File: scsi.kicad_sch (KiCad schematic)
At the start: 66 parts, among them IC107 D4364G, IC109 D6378GF, IC301 L7805, IC302 1951A, Q104 2SC2412K

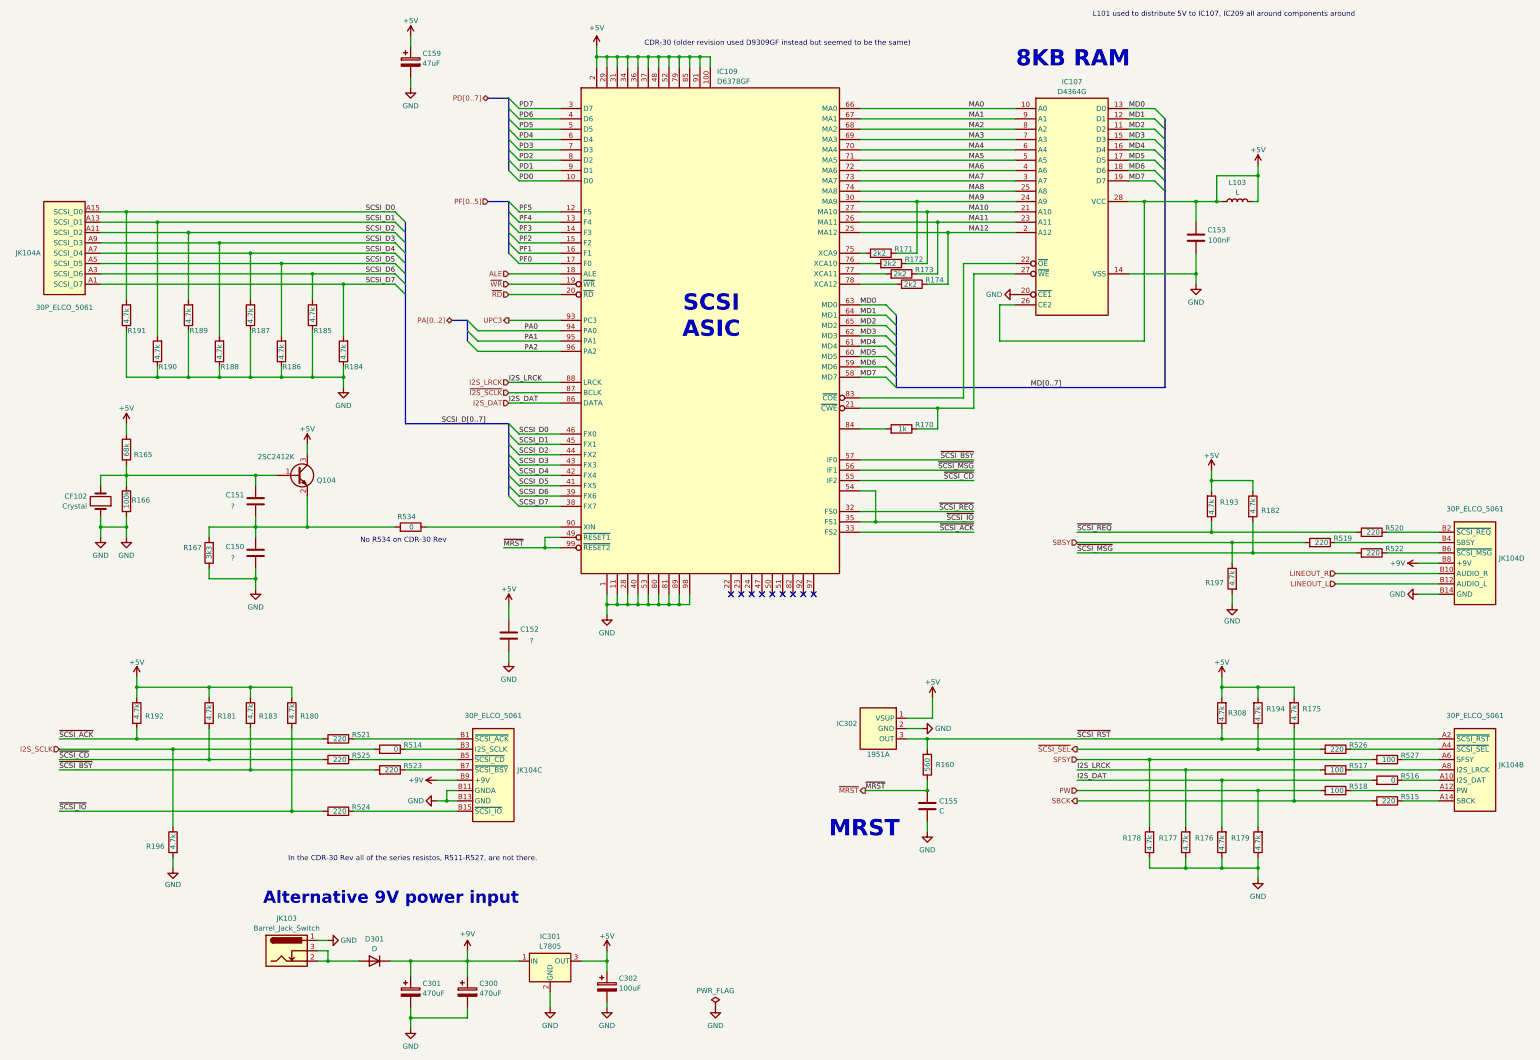
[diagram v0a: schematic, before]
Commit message: Small Schematics update to tidy signals attached to SCSI and MCU chips.
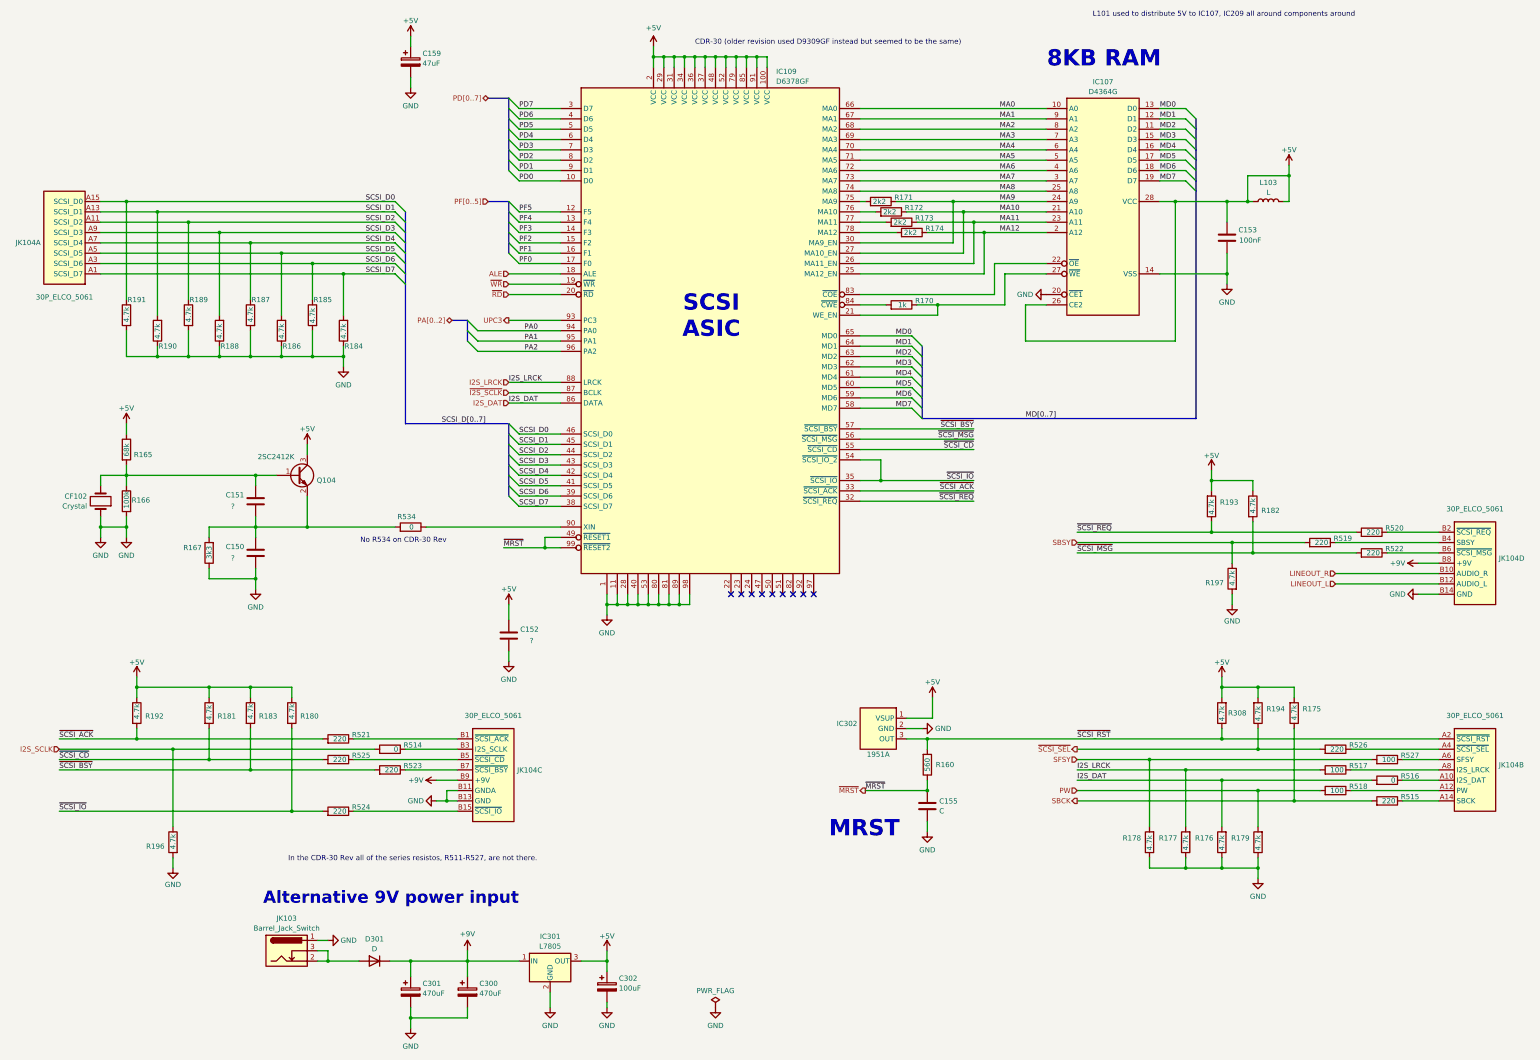
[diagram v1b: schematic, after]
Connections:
- net GND: now also R185.2, R187.2, R189.2, R191.2; no longer R185.1, R187.1, R189.1, R191.1
- net MD0: now also IC109.65 (MD0); no longer IC109.63 (MD0)
- net MD2: now also IC109.63 (MD2); no longer IC109.65 (MD2)
- net SCSI_D0: now also R191.1; no longer R191.2
- net SCSI_D2: now also R189.1; no longer R189.2
- net SCSI_D4: now also R187.1; no longer R187.2
- net SCSI_D6: now also R185.1; no longer R185.2
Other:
- moved on the sheet: C153, IC107, JK104A, L103, R170, R171, R172, R173, R174, R184, R185, R186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

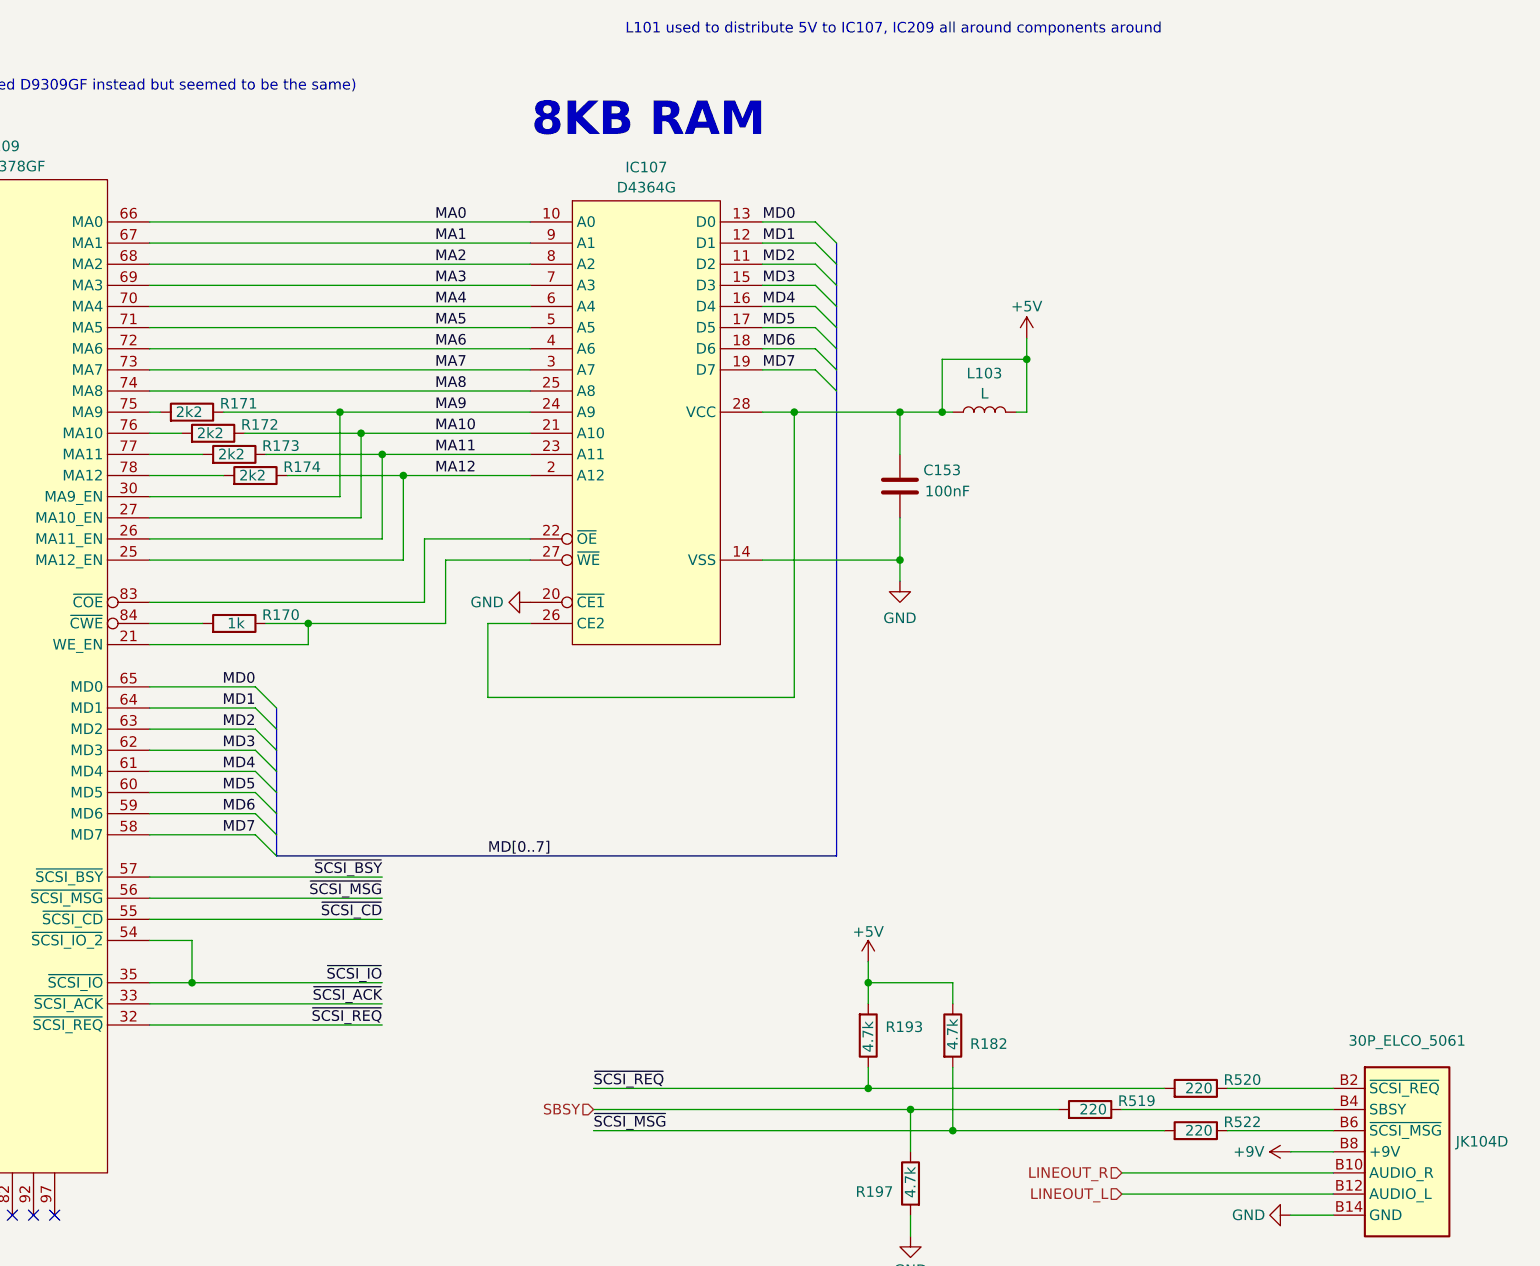
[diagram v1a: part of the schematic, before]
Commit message: KSS-220A Flexible PCBs ready and on order for trial.
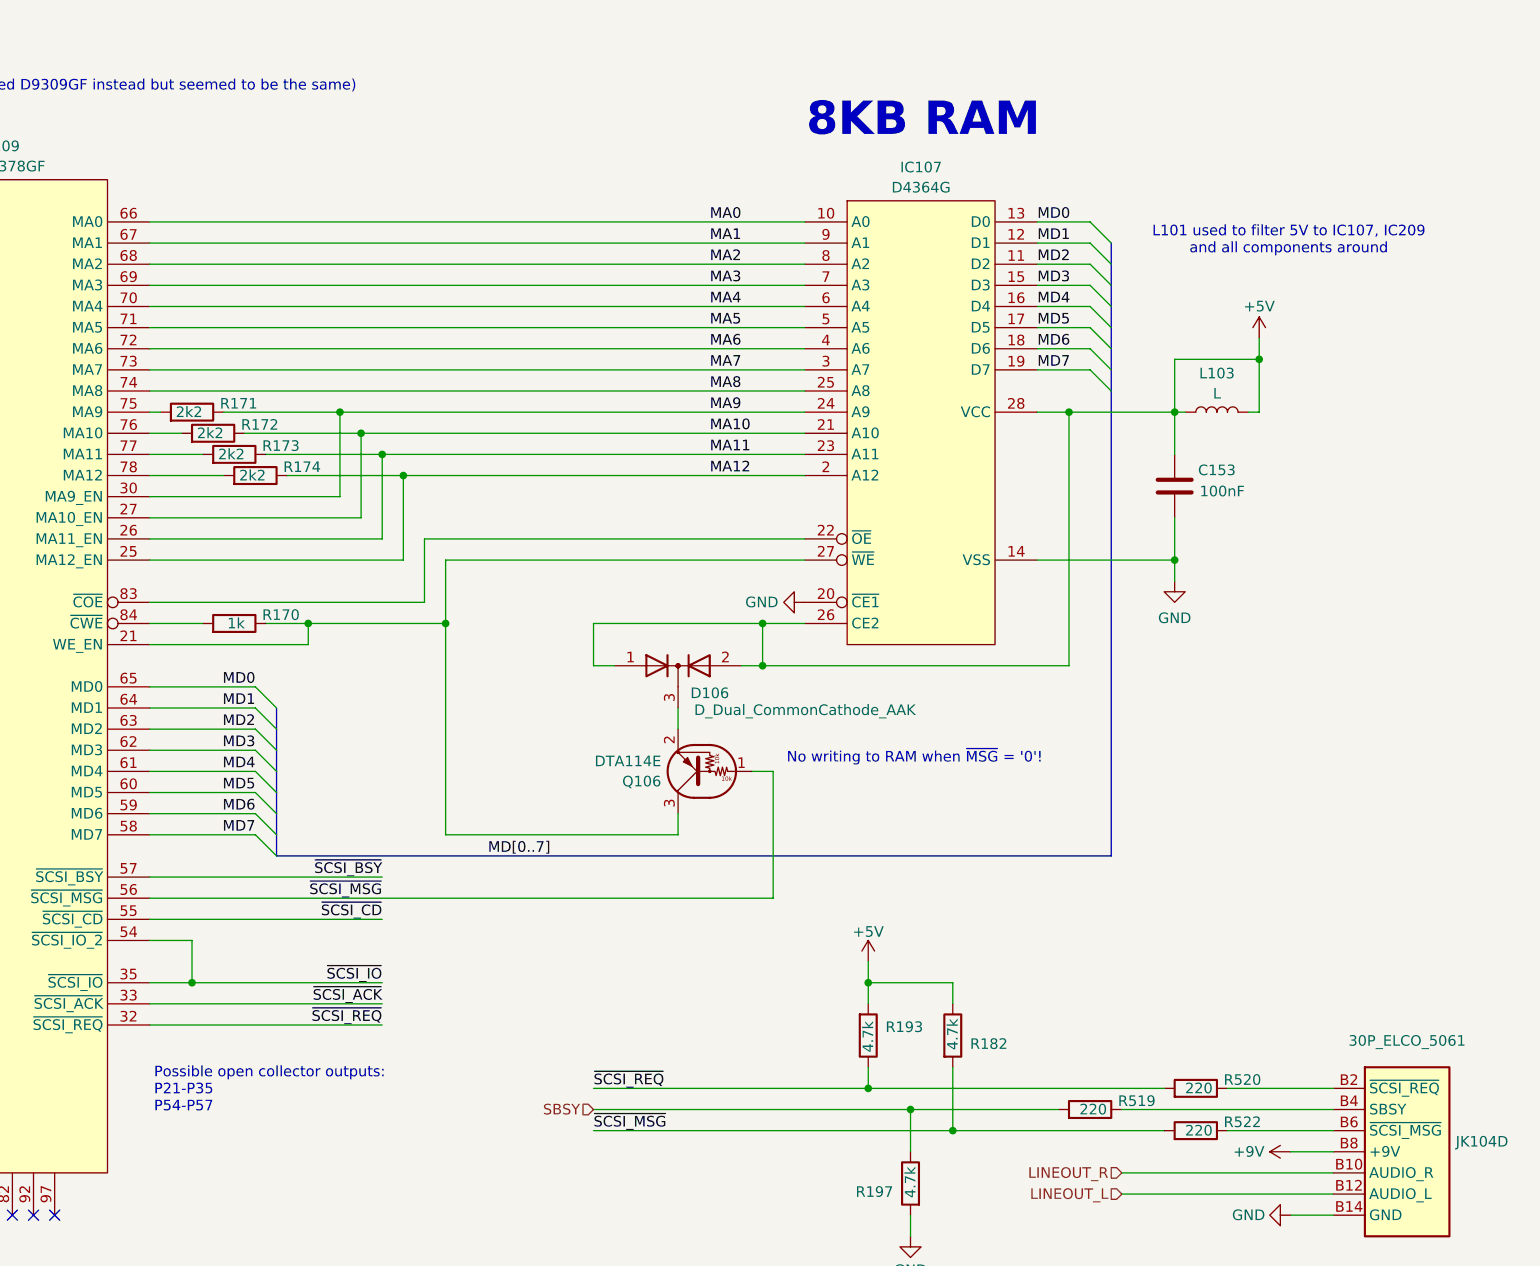
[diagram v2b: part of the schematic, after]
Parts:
- added D106: D_Dual_CommonCathode_AAK, Package_TO_SOT_SMD:SOT-23, symbol Device:D_Dual_CommonCathode_AAK
- added Q106: DTA114E, symbol Transistor_BJT:DTA114E
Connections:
- net +5V: now also D106.1 (A), D106.2 (A)
- net ~{SCSI_MSG}: now also Q106.1 (B)
- net at IC107.27 (~{WE}), IC109.21 (WE_EN), R170.1: now also Q106.3 (C)
- new net: D106.3 (K), Q106.2 (E)
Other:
- note added: "L101 used to filter 5V to IC107, IC209 and all components around"
- note added: "No writing to RAM when ~{MSG} = '0'!"
- note added: "Possible open collector outputs: P21-P35 P54-P57"
- note removed: "L101 used to distribute 5V to IC107, IC209 all around components around"
- moved on the sheet: C153, IC107, L103
